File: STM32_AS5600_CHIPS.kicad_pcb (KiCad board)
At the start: 2 copper layers, 29.6 x 37.2 mm, 39 parts, among them IC1 AS5600-ASOT, J1 Conn_01x04_Pin, J3 Conn_01x07_Pin, J4 USB4105-GF-A-120, U1 STM32F103C8Tx, U2 AMS1117-3.3, Y2 Crystal

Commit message: Add files via upload
2nd Commit
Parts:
- added G***: LOGO, LOGO, F.Cu at (183.5, 75.4)
- R7: value R -> 10k
- moved H4 2.55 mm to (174.3, 95.8)
- moved H3 2.53 mm to (202.5, 95.7)
- moved H2 2.52 mm to (202.5, 60.1)
- moved H1 2.48 mm to (174.2, 60.2)
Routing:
- net +3.3V: track 147.3 -> 141.8 mm
- net /I2C_SCL: track 20.0 -> 19.0 mm
- net /I2C_SDA: track 14.9 -> 13.9 mm
- net GND: vias 10 -> 11
- added copper zone on B.Cu, net GND
- added copper zone on F.Cu, net GND
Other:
- board size 29.6 x 37.2 mm -> 33.5 x 40.9 mm

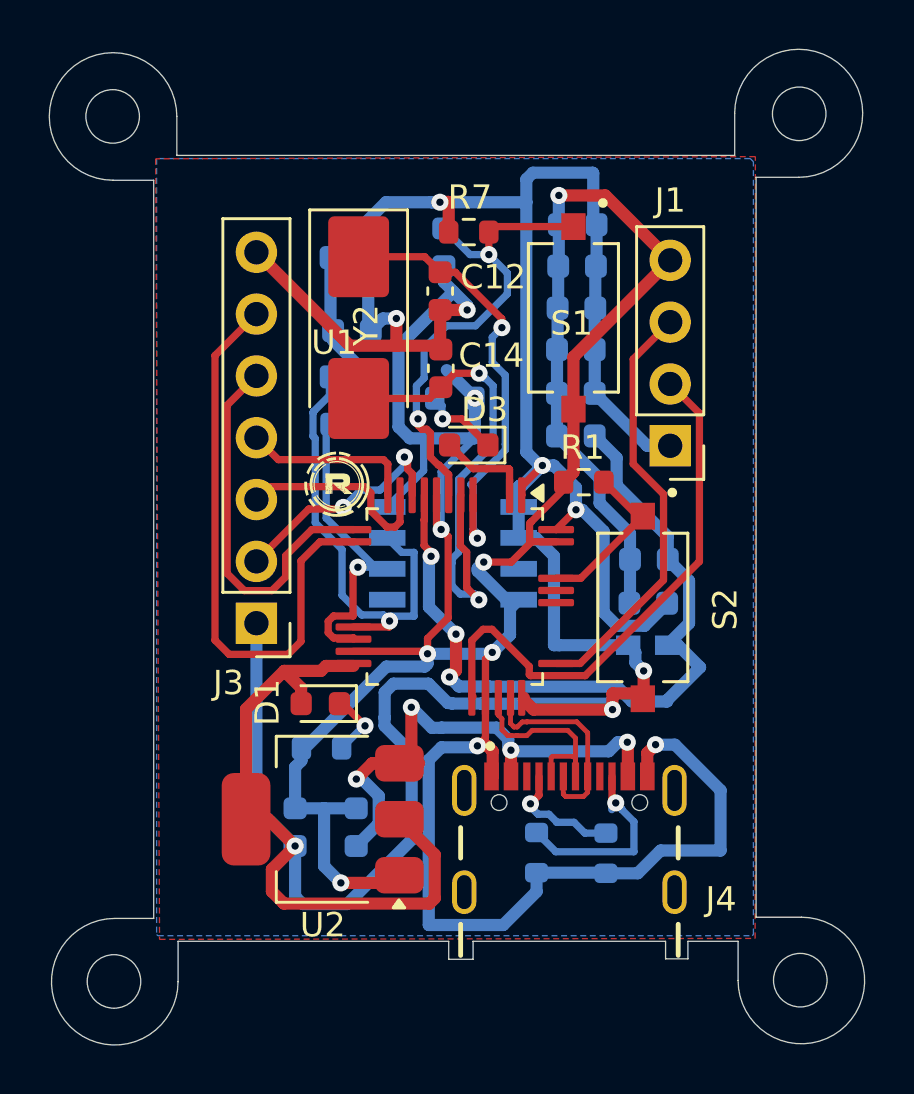
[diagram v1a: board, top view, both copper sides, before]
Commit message: Add files via upload
dfm check done commit, but usb lot idth issue
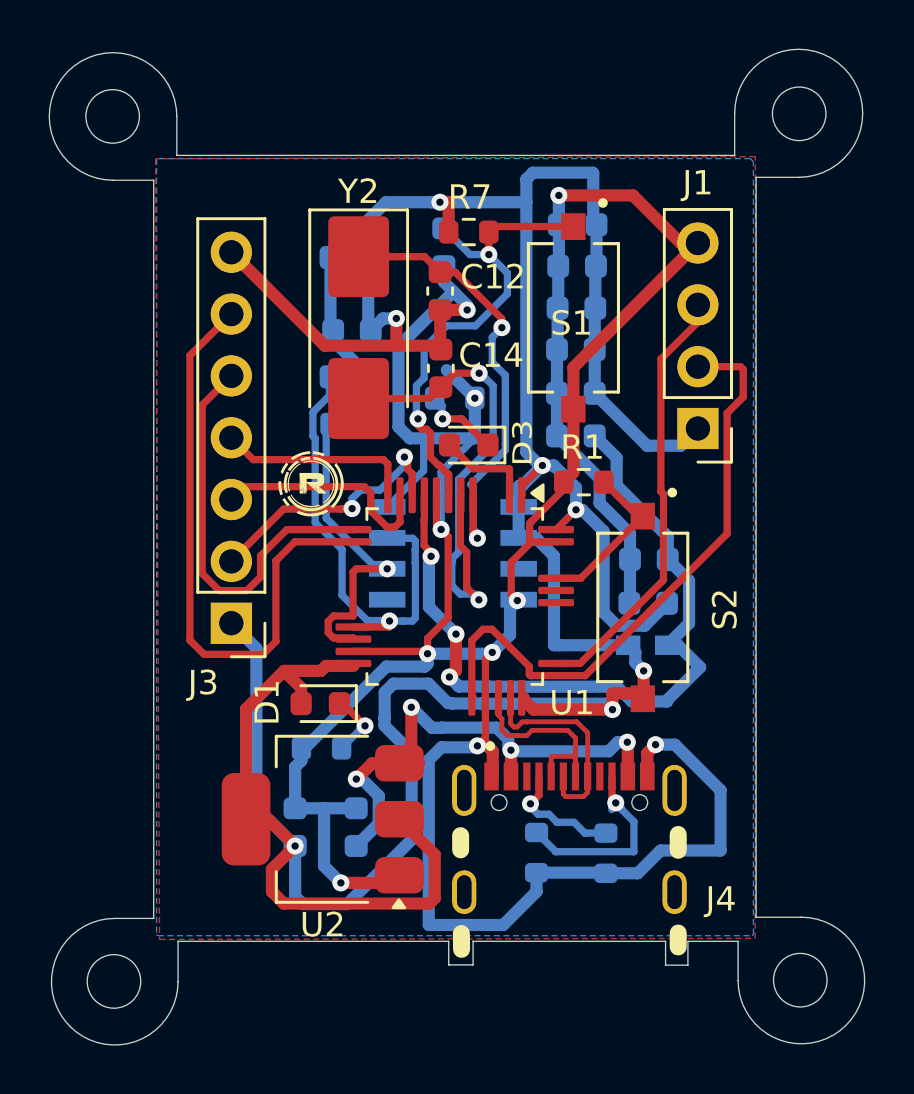
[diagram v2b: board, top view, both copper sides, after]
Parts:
- moved J1 1.34 mm to (198.3, 73.1)
- moved G*** 1.06 mm to (182.4, 75.3)
- moved J3 1.03 mm to (179.1, 81.1)
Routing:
- net /SWDIO: track 22.7 -> 25.4 mm
- net +3.3V: track 141.8 -> 143.7 mm
- net /Dummy1: track 9.77 -> 11.0 mm
- net GND: track 154.7 -> 155.7 mm
- net /Dummy4: track 15.6 -> 16.7 mm
- net /Dummy3: track 7.13 -> 8.16 mm
- net /Dummy5: track 23.9 -> 24.9 mm
- net /Dummy2: track 8.42 -> 9.45 mm
- net /I2C_SCL: track 19.0 -> 19.6 mm
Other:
- outline, holes or cut-outs redrawn

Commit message: MOUNTING HOLES UPDATED
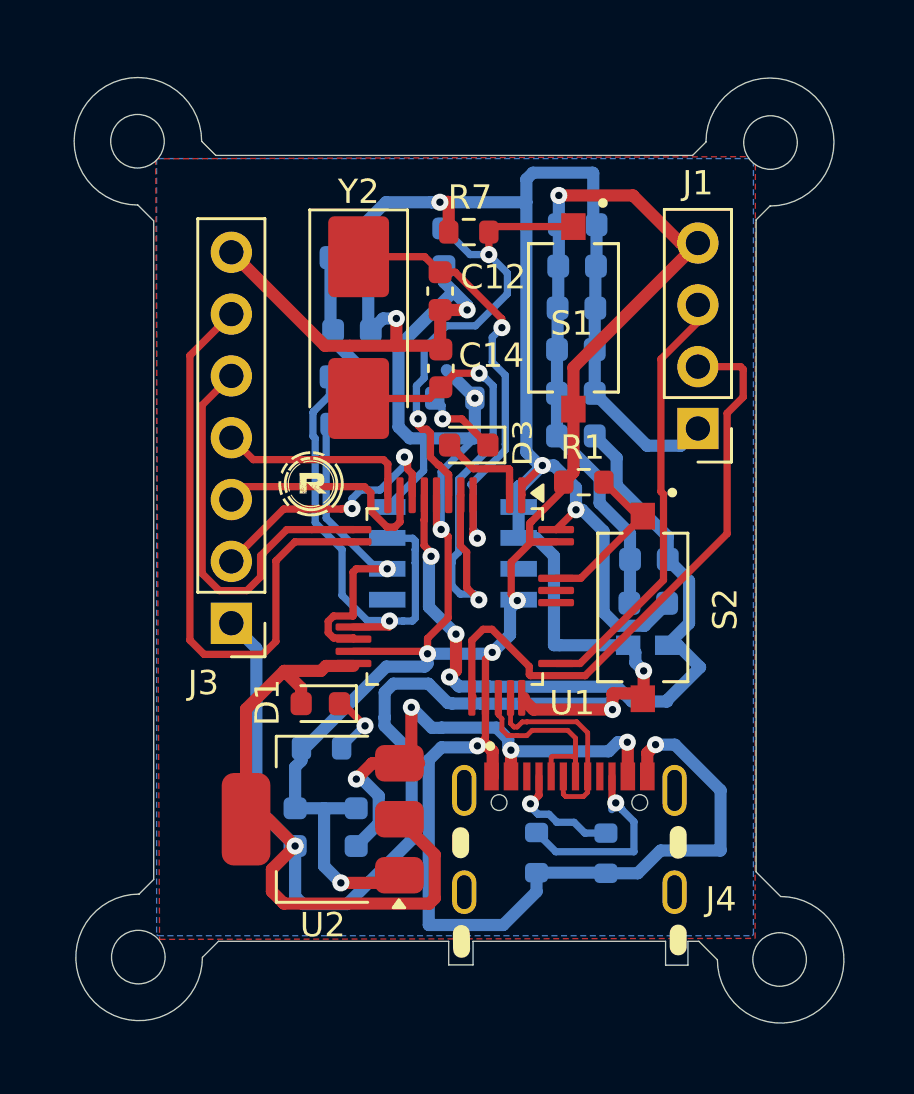
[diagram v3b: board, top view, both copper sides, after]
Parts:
- moved H2 1.67 mm to (201.3, 61.3)
- moved H1 1.44 mm to (175.3, 61.3)
- moved H4 1.41 mm to (175.3, 94.8)
- moved H3 1.20 mm to (201.6, 94.9)
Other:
- board size 33.5 x 40.9 mm -> 31.6 x 38.8 mm
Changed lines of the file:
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@@
 	(footprint "MountingHole:MountingHole_2.2mm_M2"
 		(layer "F.Cu")
-		(at 174.297737 95.789)
+		(at 175.297737 94.789)
 		(descr "Mounting Hole 2.2mm, M2, no annular, generated by kicad-footprint-generator mountinghole.py")
 		(tags "mountinghole M2")
@@
 	(footprint "MountingHole:MountingHole_2.2mm_M2"
 		(layer "F.Cu")
-		(at 202.451809 60.141106)
+		(at 201.271809 61.321106)
 		(descr "Mounting Hole 2.2mm, M2, no annular, generated by kicad-footprint-generator mountinghole.py")
 		(tags "mountinghole M2")
@@
 	(footprint "MountingHole:MountingHole_2.2mm_M2"
 		(layer "F.Cu")
-		(at 202.495837 95.73702)
+		(at 201.645837 94.88702)
 		(descr "Mounting Hole 2.2mm, M2, no annular, generated by kicad-footprint-generator mountinghole.py")
 		(tags "mountinghole M2")
@@
 	(footprint "MountingHole:MountingHole_2.2mm_M2"
 		(layer "F.Cu")
-		(at 174.242789 60.248205)
+		(at 175.262789 61.268205)
 		(descr "Mounting Hole 2.2mm, M2, no annular, generated by kicad-footprint-generator mountinghole.py")
 		(tags "mountinghole M2")
@@
 	)
 	(gr_line
-		(start 176.880305 60.25)
-		(end 176.880305 61.85)
+		(start 201.69 92.3)
+		(end 200.68 91.29)
 		(stroke
 			(width 0.05)
@@
 	)
 	(gr_arc
-		(start 199.799981 60.12)
-		(mid 204.289704 58.260296)
-		(end 202.43 62.750019)
+		(start 198.619981 61.3)
+		(mid 203.109704 59.440296)
+		(end 201.25 63.930019)
 		(stroke
 			(width 0.05)
@@
 	)
 	(gr_line
-		(start 176.930173 94.14)
+		(start 178.590173 94.14)
 		(end 188.05 94.14)
 		(stroke
@@
 	)
 	(gr_line
-		(start 199.94 94.14)
+		(start 198.33 94.14)
 		(end 197.88 94.14)
 		(stroke
@@
 	)
 	(gr_arc
-		(start 174.26 62.870305)
-		(mid 172.407165 58.397165)
-		(end 176.880305 60.25)
+		(start 175.28 63.890305)
+		(mid 173.427165 59.417165)
+		(end 177.900305 61.27)
 		(stroke
 			(width 0.05)
@@
 		(layer "Edge.Cuts")
 	)
-	(gr_arc
-		(start 176.930173 95.8)
-		(mid 172.4914 97.6386)
-		(end 174.33 93.199827)
+	(gr_line
+		(start 199.09 94.9)
+		(end 198.33 94.14)
 		(stroke
 			(width 0.05)
@@
 		(layer "Edge.Cuts")
 	)
-	(gr_line
-		(start 176.930173 95.8)
-		(end 176.930173 94.14)
+	(gr_arc
+		(start 177.930173 94.8)
+		(mid 173.4914 96.6386)
+		(end 175.33 92.199827)
 		(stroke
 			(width 0.05)
@@
 	)
 	(gr_line
-		(start 174.33 93.199827)
-		(end 175.93 93.199827)
+		(start 175.33 92.199827)
+		(end 175.93 91.599827)
 		(stroke
 			(width 0.05)
@@
 	)
 	(gr_arc
-		(start 202.54 93.15)
-		(mid 204.378478 97.588478)
-		(end 199.94 95.75)
+		(start 201.69 92.3)
+		(mid 203.528478 96.738478)
+		(end 199.09 94.9)
 		(stroke
 			(width 0.05)
@@
 	)
 	(gr_line
-		(start 202.54 93.15)
-		(end 200.68 93.15)
+		(start 189.05 95.11)
+		(end 189.05 94.14)
 		(stroke
 			(width 0.05)
@@
 	)
 	(gr_line
-		(start 189.05 95.11)
-		(end 189.05 94.14)
+		(start 175.28 63.890305)
+		(end 175.93 64.540305)
 		(stroke
 			(width 0.05)
@@
 	)
 	(gr_line
-		(start 202.43 62.750019)
-		(end 200.68 62.750019)
+		(start 198.619981 61.3)
+		(end 198.069981 61.85)
 		(stroke
 			(width 0.05)
@@
 	)
 	(gr_line
-		(start 174.26 62.870305)
-		(end 175.93 62.870305)
+		(start 177.930173 94.8)
+		(end 178.59 94.140173)
 		(stroke
 			(width 0.05)
@@
 	)
 	(gr_line
-		(start 197.88 95.12)
-		(end 197.88 94.14)
+		(start 201.25 63.930019)
+		(end 200.68 64.500019)
 		(stroke
 			(width 0.05)
@@
 	)
 	(gr_line
-		(start 199.94 95.75)
-		(end 199.94 94.14)
+		(start 177.900305 61.27)
+		(end 178.48 61.849695)
 		(stroke
 			(width 0.05)
@@
 	)
 	(gr_line
-		(start 200.68 93.15)
-		(end 200.68 62.750019)
+		(start 197.88 95.12)
+		(end 197.88 94.14)
 		(stroke
 			(width 0.05)
@@
 	)
 	(gr_line
-		(start 199.799981 61.85)
-		(end 176.88 61.85)
+		(start 200.68 91.29)
+		(end 200.68 64.500019)
 		(stroke
 			(width 0.05)
@@
 	)
 	(gr_line
-		(start 175.93 62.870305)
-		(end 175.93 93.199827)
+		(start 198.069981 61.85)
+		(end 178.48 61.85)
 		(stroke
 			(width 0.05)
@@
 	)
 	(gr_line
-		(start 189.05 94.14)
-		(end 196.96 94.14)
+		(start 175.93 64.54)
+		(end 175.93 91.599827)
 		(stroke
 			(width 0.05)
@@
 	)
 	(gr_line
-		(start 199.799981 60.12)
-		(end 199.799981 61.85)
+		(start 189.05 94.14)
+		(end 196.96 94.14)
 		(stroke
 			(width 0.05)
